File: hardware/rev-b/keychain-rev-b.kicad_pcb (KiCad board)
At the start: 4 copper layers, 30 x 52.5 mm, 62 parts, among them J1 USB-C, J2 OLED 0.96" I2C, J3 SWD, M1 вибромотор 0820, Q1 AO3401A, Q2 AO3401A, Q3 AO3400A, Q4 AO3400A, SW1 B3U-3100P, U1 MDBT50Q-1MV2, U2 MCP73832-2, U3 USBLC6-2SC6, U4 LIS3DH, U5 LTR-303ALS-01, U6 SPH0641LM4H-1

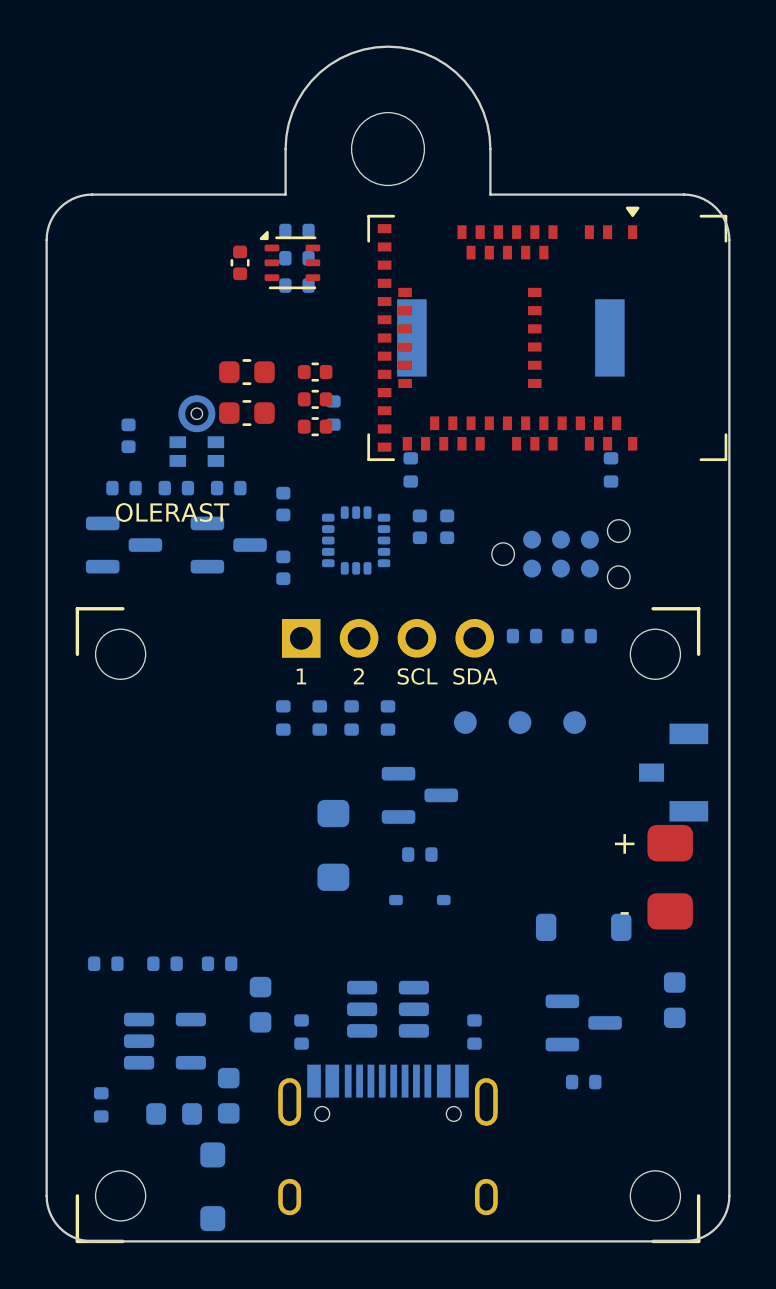
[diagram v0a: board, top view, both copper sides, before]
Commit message: Черновик: промежуточные правки исполнителей (в работе)
Прошивка, симулятор, движок, корпус и документы — состояние на сейчас. Плата выбирается
из двух вариантов разводки, файлы для завода ещё старые.

Co-Authored-By: Claude Opus 5.5 <noreply@anthropic.com>
Claude-Session: https://claude.ai/code/session_01RQ7GfaTDyVK1Dcdo3sKM8F
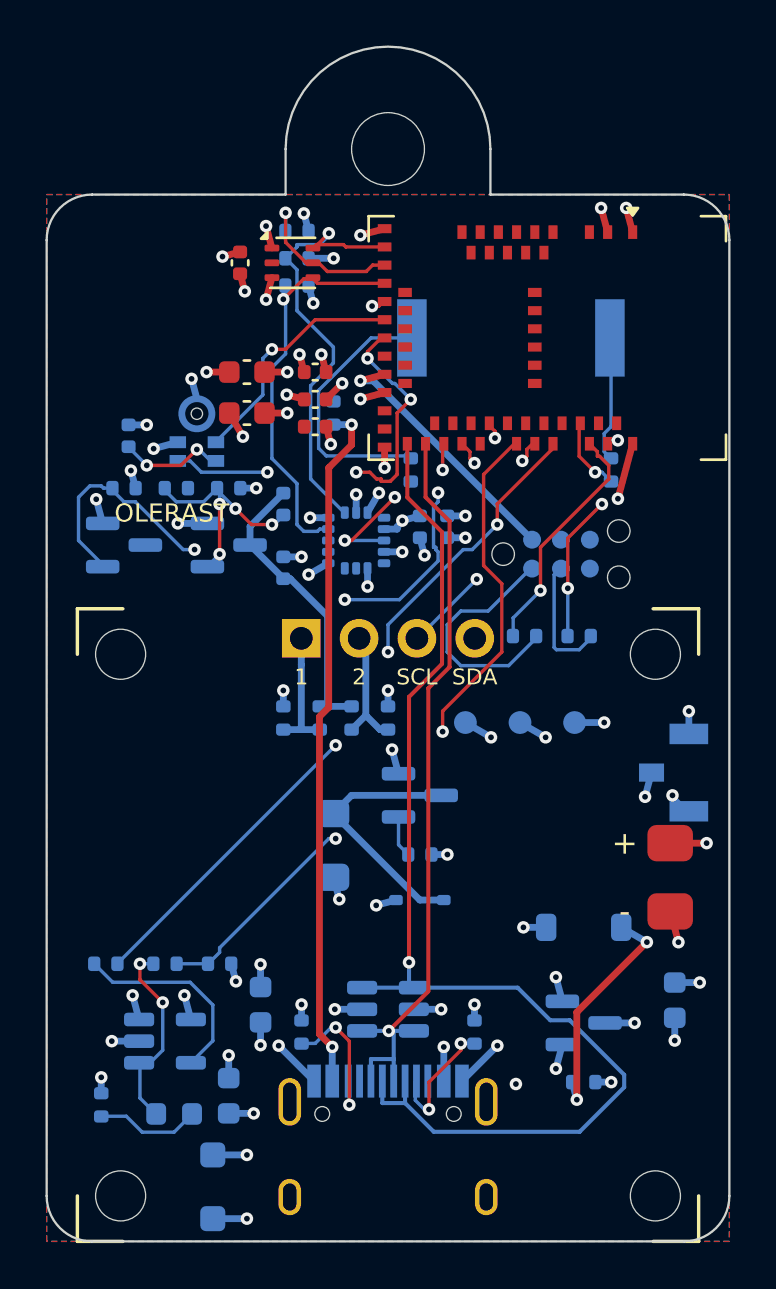
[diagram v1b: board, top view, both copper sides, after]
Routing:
- net VBUS: track 0.00 -> 115.1 mm, vias 0 -> 11
- net VDD: track 0.00 -> 83.2 mm, vias 0 -> 15
- net VSYS: track 0.00 -> 71.2 mm, vias 0 -> 11
- net VBAT: track 0.00 -> 56.2 mm, vias 0 -> 4
- net USB_DN: track 0.00 -> 52.7 mm, vias 0 -> 1
- net GND: track 0.00 -> 45.2 mm, vias 0 -> 43
- net USB_DP: track 0.00 -> 33.8 mm, vias 0 -> 1
- net DISP_EN: track 0.00 -> 31.2 mm, vias 0 -> 4
- net CHG_EN: track 0.00 -> 31.1 mm, vias 0 -> 3
- net CHG_IO: track 0.00 -> 30.8 mm, vias 0 -> 2
- net SENS_SDA: track 0.00 -> 19.6 mm, vias 0 -> 1
- net BTN: track 0.00 -> 19.5 mm, vias 0 -> 2
- net SENS_SCL: track 0.00 -> 18.5 mm, vias 0 -> 1
- net PDM_DATA: track 0.00 -> 17.7 mm, vias 0 -> 4
- net ACC_INT1: track 0.00 -> 14.2 mm, vias 0 -> 3
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- added copper zone on B.Cu, net GND
- added copper zone on F.Cu, net GND
- added copper zone on In1.Cu, net GND
- added copper zone on In2.Cu, net GND

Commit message: Черновик: плата rev B — итоговая трассировка (TVS D3, CHG_EN P0.24, 47k, C6 4.7 мкФ), выходные файлы заново (в работе)
Co-Authored-By: Claude Opus 5.5 <noreply@anthropic.com>
Claude-Session: https://claude.ai/code/session_01RQ7GfaTDyVK1Dcdo3sKM8F
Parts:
- removed R21: 10R, Resistor_SMD:R_0402_1005Metric
- removed R22, R23: 100R, Resistor_SMD:R_0402_1005Metric
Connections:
- C8 pad 1: VBUS_NRF -> VBUS
- J3 pad 2: SWDIO_J -> SWDIO
- J3 pad 4: SWDCLK_J -> SWDCLK
- U1 pad 32: VBUS_NRF -> VBUS
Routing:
- net VIB_EN: track 1.83 -> 23.0 mm, vias 0 -> 1
- net VSYS: track 71.2 -> 86.6 mm
- net MIC_PWR: track 4.69 -> 18.0 mm, vias 2 -> 1
- net ACC_INT1: track 14.2 -> 25.4 mm, vias 3 -> 2
- net SWDIO_J: track 10.7 -> 0.00 mm
- net DISP_EN: track 31.2 -> 40.5 mm, vias 4 -> 1
- net BUZ_A_IO: track 0.00 -> 9.10 mm, vias 0 -> 1
- net DISP_G: track 10.4 -> 18.0 mm, vias 4 -> 2
- net ACC_INT2: track 0.00 -> 7.15 mm, vias 0 -> 1
- net CHG_EN: track 31.1 -> 38.2 mm, vias 3 -> 1
- net CHG_IO: track 30.8 -> 37.9 mm, vias 2 -> 1
- net VDD: track 83.2 -> 90.3 mm, vias 15 -> 16
- net BUZ_A: track 11.8 -> 5.31 mm
- net SENS_SCL: track 18.5 -> 24.5 mm, vias 1 -> 2
- net SWDCLK_J: track 5.62 -> 0.00 mm
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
